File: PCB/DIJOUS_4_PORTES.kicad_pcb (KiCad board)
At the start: 2 copper layers, 180.4 x 120 mm, 63 parts, among them J1 PowerIN, J10 DOOR_LCK, J12 WIN_SW, J14 FINAL_CARRERA_UP, J15 FINAL_CARRERA_DOWN, J2 OUT_WIN, J3 ICSP, J4 CAN, J5 OUT_DOOR, J6 USART, J7 SPI, J8 RFID_COAX, SW1 DOOR_LCK, SW3 WIN_SW, U1 LT1528CT-PBF, U2 PIC32MK0256MCJ048-I/Y8X, U3 TCAN334D, U4 MAX22201ATC+, U5 MAX22201ATC+, Y1 ASZKDV-32.768KHZ-L-T3, Y2 ECS-3225SMV-080-GP-TR

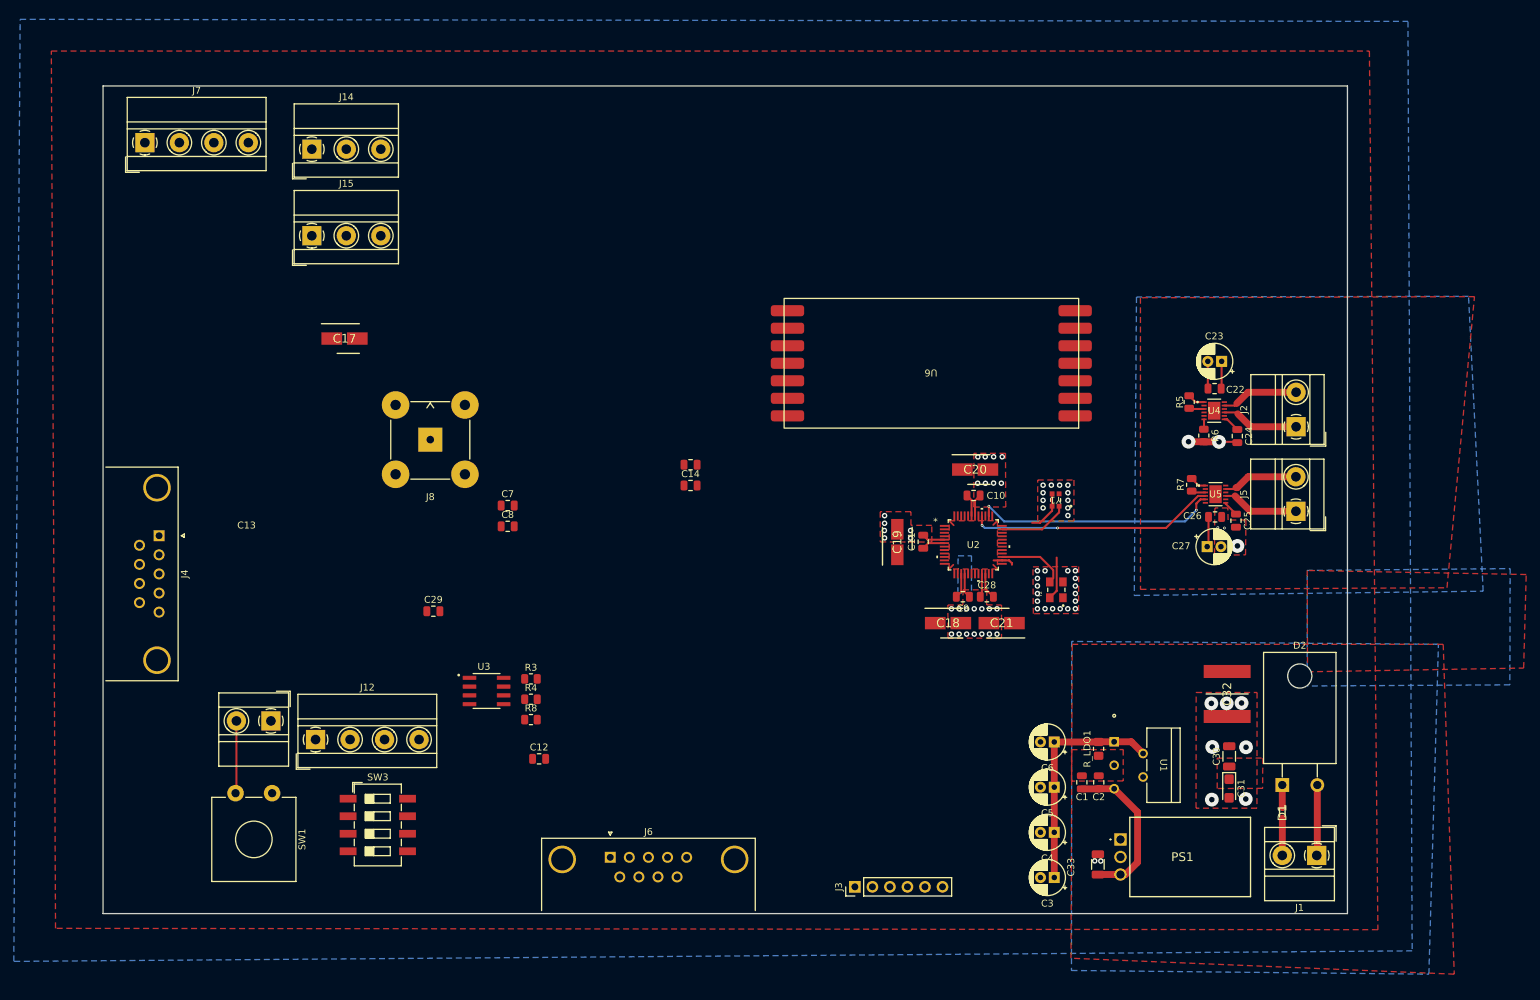
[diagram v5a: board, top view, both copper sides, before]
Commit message: first PCB done, need to correct vias and solve all DRC errors
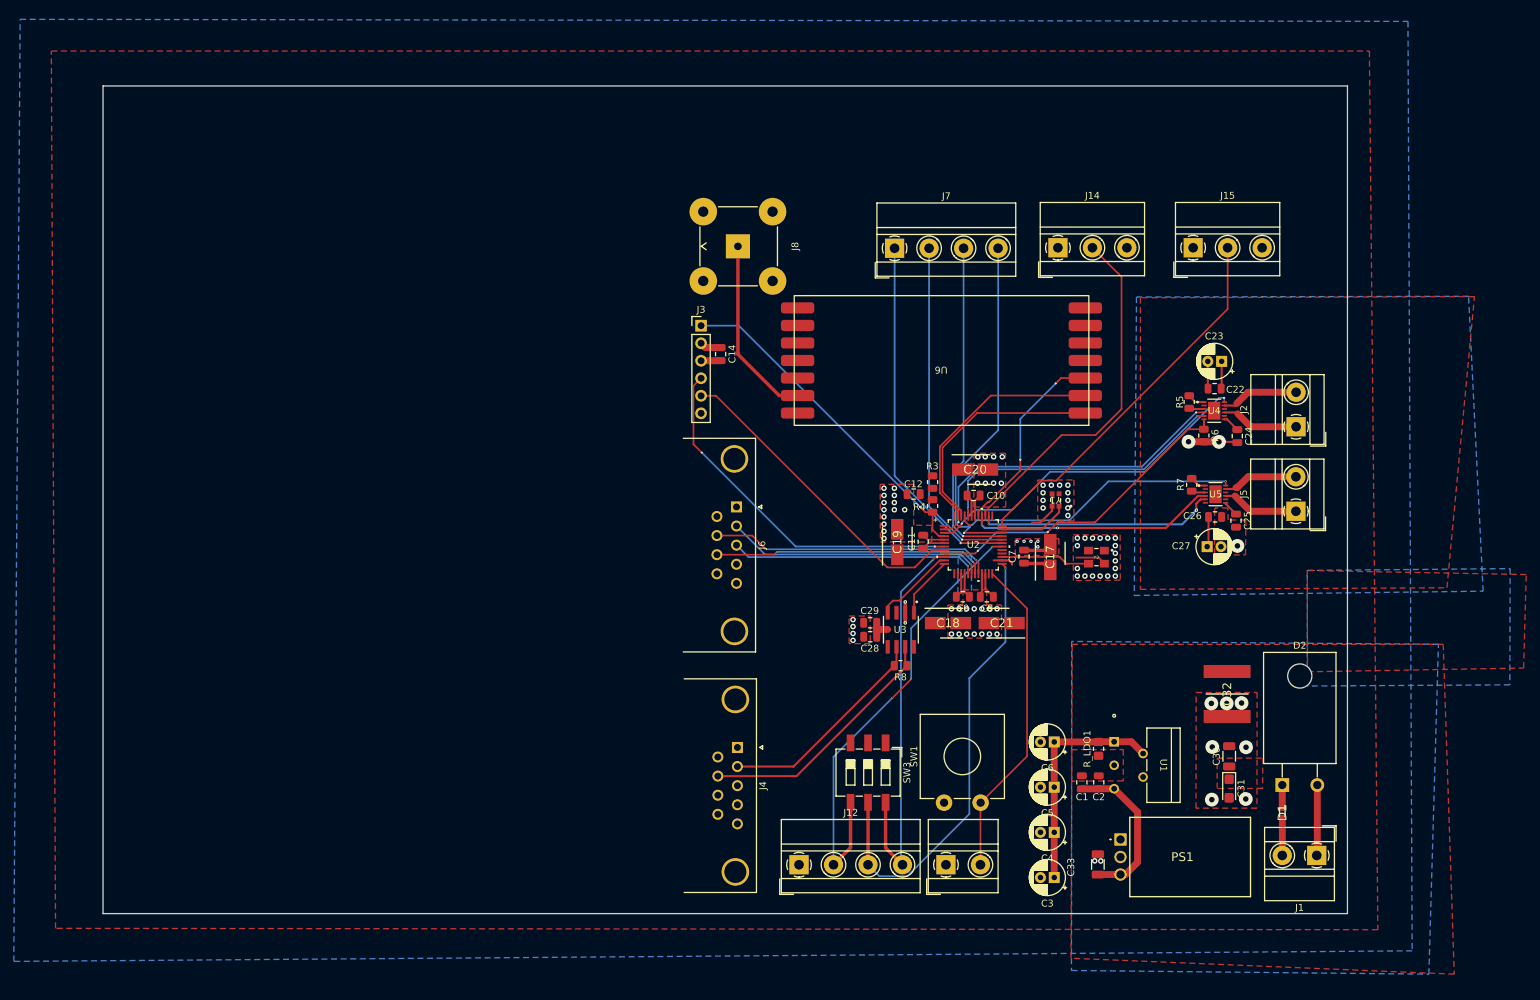
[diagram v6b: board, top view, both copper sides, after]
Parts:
- removed C13: 100n, Capacitor_SMD:C_0805_2012Metric
- SW3: footprint Button_Switch_SMD:SW_DIP_SPSTx04_Slide_6.7x11.72mm_W8.61mm_P2.54mm_LowProfile -> Button_Switch_SMD:SW_DIP_SPSTx03_Slide_6.7x9.18mm_W8.61mm_P2.54mm_LowProfile
- moved J15 127.8 mm to (218.2, 63.5)
- moved J7 109.7 mm to (174.9, 63.5)
- moved J14 109.1 mm to (198.6, 63.5)
- moved C17 107.1 mm to (197.5, 108.3), turned to 90 degrees
- moved J10 100.0 mm to (182.3, 152.9), turned to 0 degrees
- moved SW1 97.4 mm to (182.1, 143.9), turned to 90 degrees
- moved J4 89.3 mm to (152.1, 135.9)
- moved J3 84.3 mm to (146.8, 74.8), turned to 0 degrees
- moved C7 75.2 mm to (193.7, 108.2), turned to 90 degrees
- moved J12 72.4 mm to (161.1, 152.9)
- moved SW3 71.5 mm to (171.1, 139.5), turned to -90 degrees
- moved C8 70.2 mm to (188.3, 114.1), turned to 180 degrees
- moved C12 66.5 mm to (177.7, 99.2), turned to 180 degrees
- moved R3 64.8 mm to (180.4, 97.4), turned to 90 degrees
- moved R4 64.6 mm to (180.4, 100.9), turned to 90 degrees
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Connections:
- C1 pad 2: GNDPWR -> GND
- C2 pad 2: GNDPWR -> GND
- C33 pad 2: GNDPWR -> GND
- J3 pad 3: Net-(J3-VSS) -> GND
- J7 pad 1: SPI_CK -> SPI_SS
- J7 pad 2: SPI_SDI -> SPI_SDO
- J7 pad 3: SPI_SDO -> SPI_SDI
- J7 pad 4: SPI_SS -> SPI_CK
- R_LDO1 pad 1: GNDPWR -> GND
- SW3 pad 4: WIN_SW3 -> WIN_SW1
- SW3 pad 6: WIN_SW1 -> WIN_SW3
- U1 pad 3: GNDPWR -> GND
- U2 pad 1: TCK -> unconnected-(U2-TCK/RPA7/PWM4L/RA7-Pad1)
- U2 pad 17: UART_RX -> UART_TX
- U2 pad 18: UART_TX -> UART_RX
- U2 pad 23: TDI -> unconnected-(U2-TDI/DAC2/AN26/CVD26/RPA8/SDA2/RA8-Pad23)
- U2 pad 37: TMS -> unconnected-(U2-TMS/OA5IN-/AN27/CVD27/LVDIN/C5IN1-/RPB9/RB9-Pad37)
- U2 pad 44: RFID_OUT -> WIN_IN2
- U2 pad 45: RFID_IN -> /FAULT_DOOR
- U2 pad 46: WIN_IN2 -> RFID_IN
- U2 pad 47: /FAULT_DOOR -> RFID_OUT
- U2 pad 48: TDO -> unconnected-(U2-TDO/PWM4H/RA10-Pad48)
- U2 pad 7: PGECx -> PGEDx
- U2 pad 8: PGEDx -> PGECx
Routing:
- net WIN_SW1: track 0.00 -> 67.1 mm, vias 0 -> 3
- net WIN_SW2: track 0.00 -> 66.8 mm, vias 0 -> 1
- net WIN_SW3: track 0.00 -> 57.7 mm, vias 0 -> 1
- net FINAL_CARRERA_DOWN: track 0.00 -> 55.1 mm
- net SPI_SS: track 0.00 -> 53.0 mm, vias 0 -> 1
- net PGEDx: track 0.00 -> 52.6 mm, vias 0 -> 2
- net FINAL_CARRERA_UP: track 0.00 -> 51.7 mm
- net SPI_CK: track 0.00 -> 51.5 mm, vias 0 -> 1
- net SPI_SDO: track 0.00 -> 50.0 mm, vias 0 -> 1
- net /MCLR: track 0.00 -> 49.5 mm, vias 0 -> 1
- net /FAULT_WIN: track 0.00 -> 49.3 mm, vias 0 -> 2
- net SPI_SDI: track 0.00 -> 48.6 mm, vias 0 -> 1
- net WIN_IN1: track 0.00 -> 47.6 mm, vias 0 -> 2
- net PGECx: track 0.00 -> 46.7 mm
- net ISEN_WIN: track 1.45 -> 46.7 mm, vias 0 -> 2
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
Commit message: correccions diverses
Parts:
- added C25: 1u, Capacitor_SMD:C_0805_2012Metric, F.Cu at (224.4, 90.8)
- added REF**: MountingHole_3.2mm_M3, MountingHole:MountingHole_3.2mm_M3, F.Cu at (160.0, 132.0)
- added REF**: MountingHole_3.2mm_M3, MountingHole:MountingHole_3.2mm_M3, F.Cu at (235.9, 62.3)
- added REF**: MountingHole_3.2mm_M3, MountingHole:MountingHole_3.2mm_M3, F.Cu at (198.6, 116.6)
- added REF**: MountingHole_3.2mm_M3, MountingHole:MountingHole_3.2mm_M3, F.Cu at (230.6, 116.9)
- added REF**: MountingHole_3.2mm_M3, MountingHole:MountingHole_3.2mm_M3, F.Cu at (166.0, 63.2)
- moved J2 0.17 mm to (233.1, 89.6)
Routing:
- net +5V: track 23.3 -> 21.9 mm
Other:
- board size 180.4 x 120 mm -> 96.9 x 106.2 mm
- board text added: "MAX22201ATC+"

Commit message: correccions de pista
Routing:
- net SPI_CK: track 51.5 -> 49.8 mm
